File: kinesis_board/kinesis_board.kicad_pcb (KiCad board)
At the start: 2 copper layers, 106.7 x 144.8 mm, 40 parts, among them J1 RIGHT_13_TOP, J10 LEFT_13_DOWN, J2 RIGHT_13_DOWN, J3 THUMB_RIGHT_SPC_KB600, J4 THUMB_RIGHT_SPC, J5 THUMB_LEFT_BAK, J6 THUMB_LEFT_BAK_KB600, J7 LEFT_1x24, J8 RIGHT_1x24, J9 LEFT_13_TOP

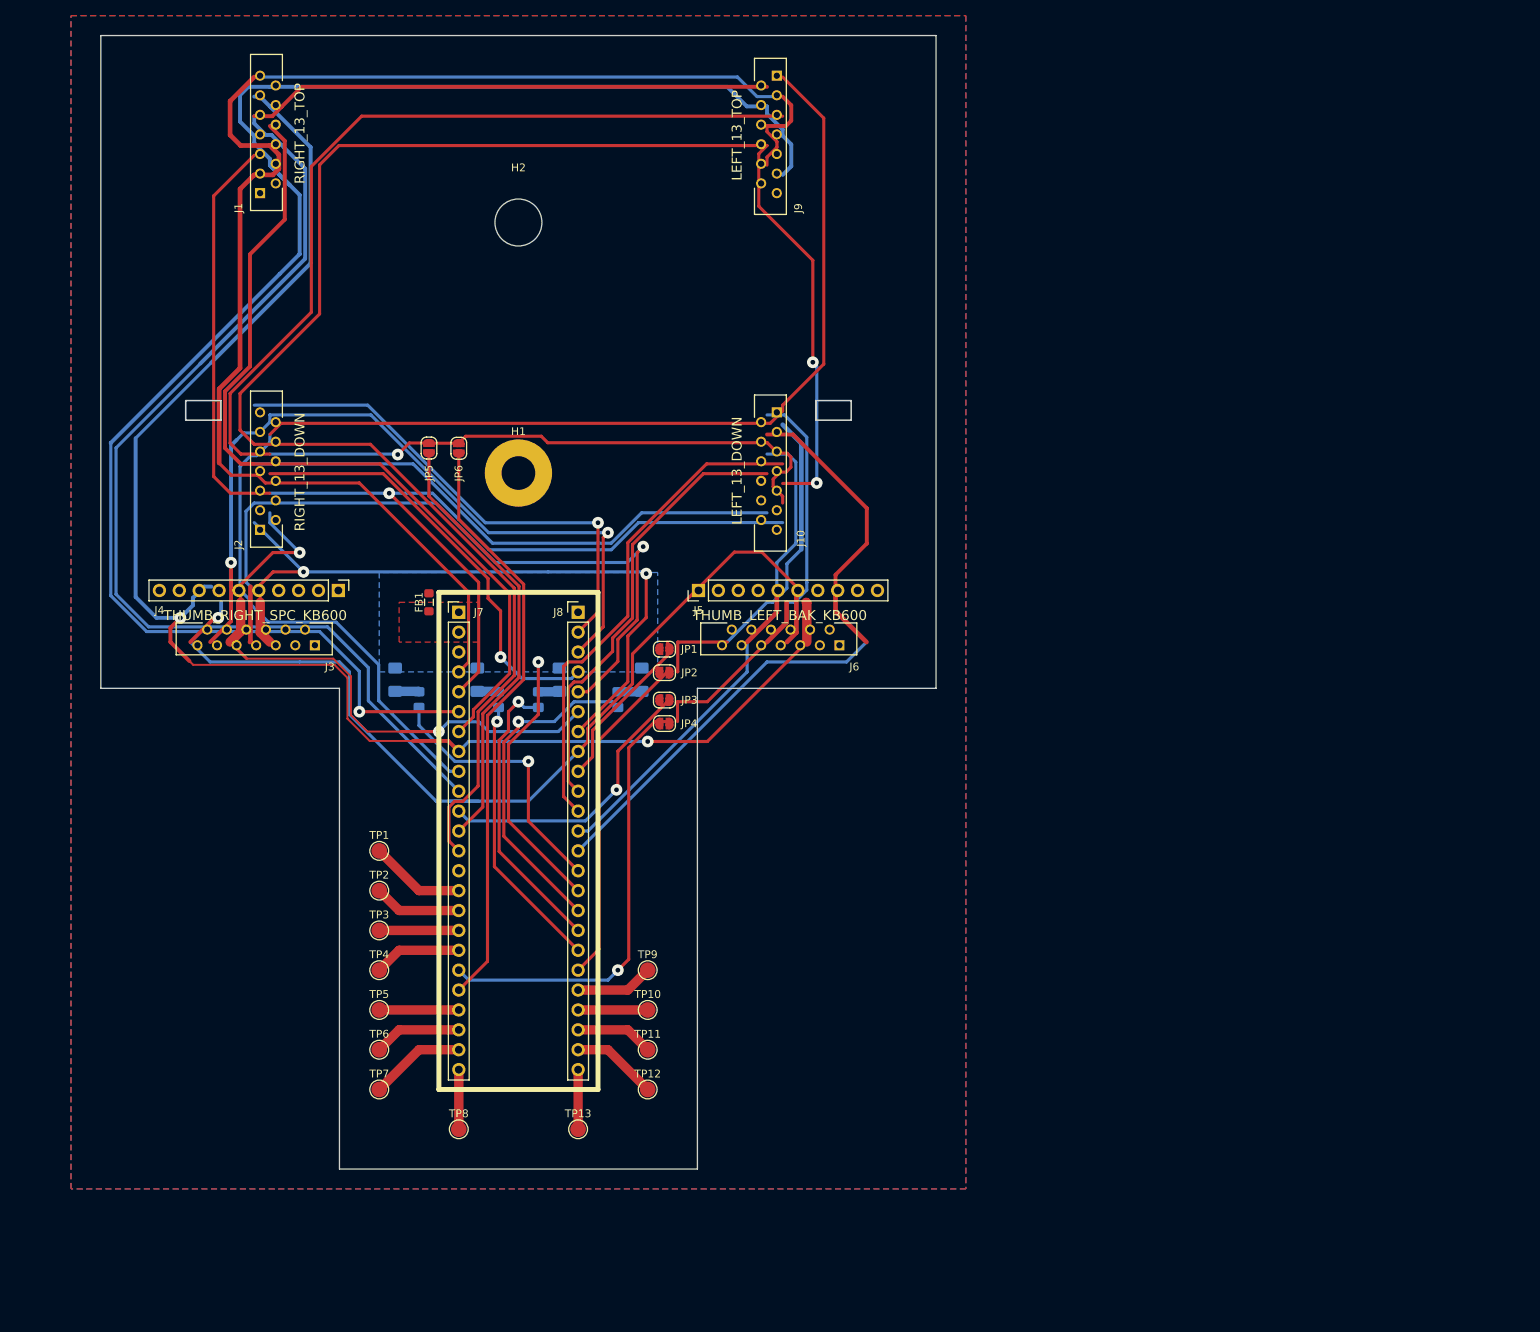
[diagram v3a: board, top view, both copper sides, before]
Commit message: finished routing of revision 2.0
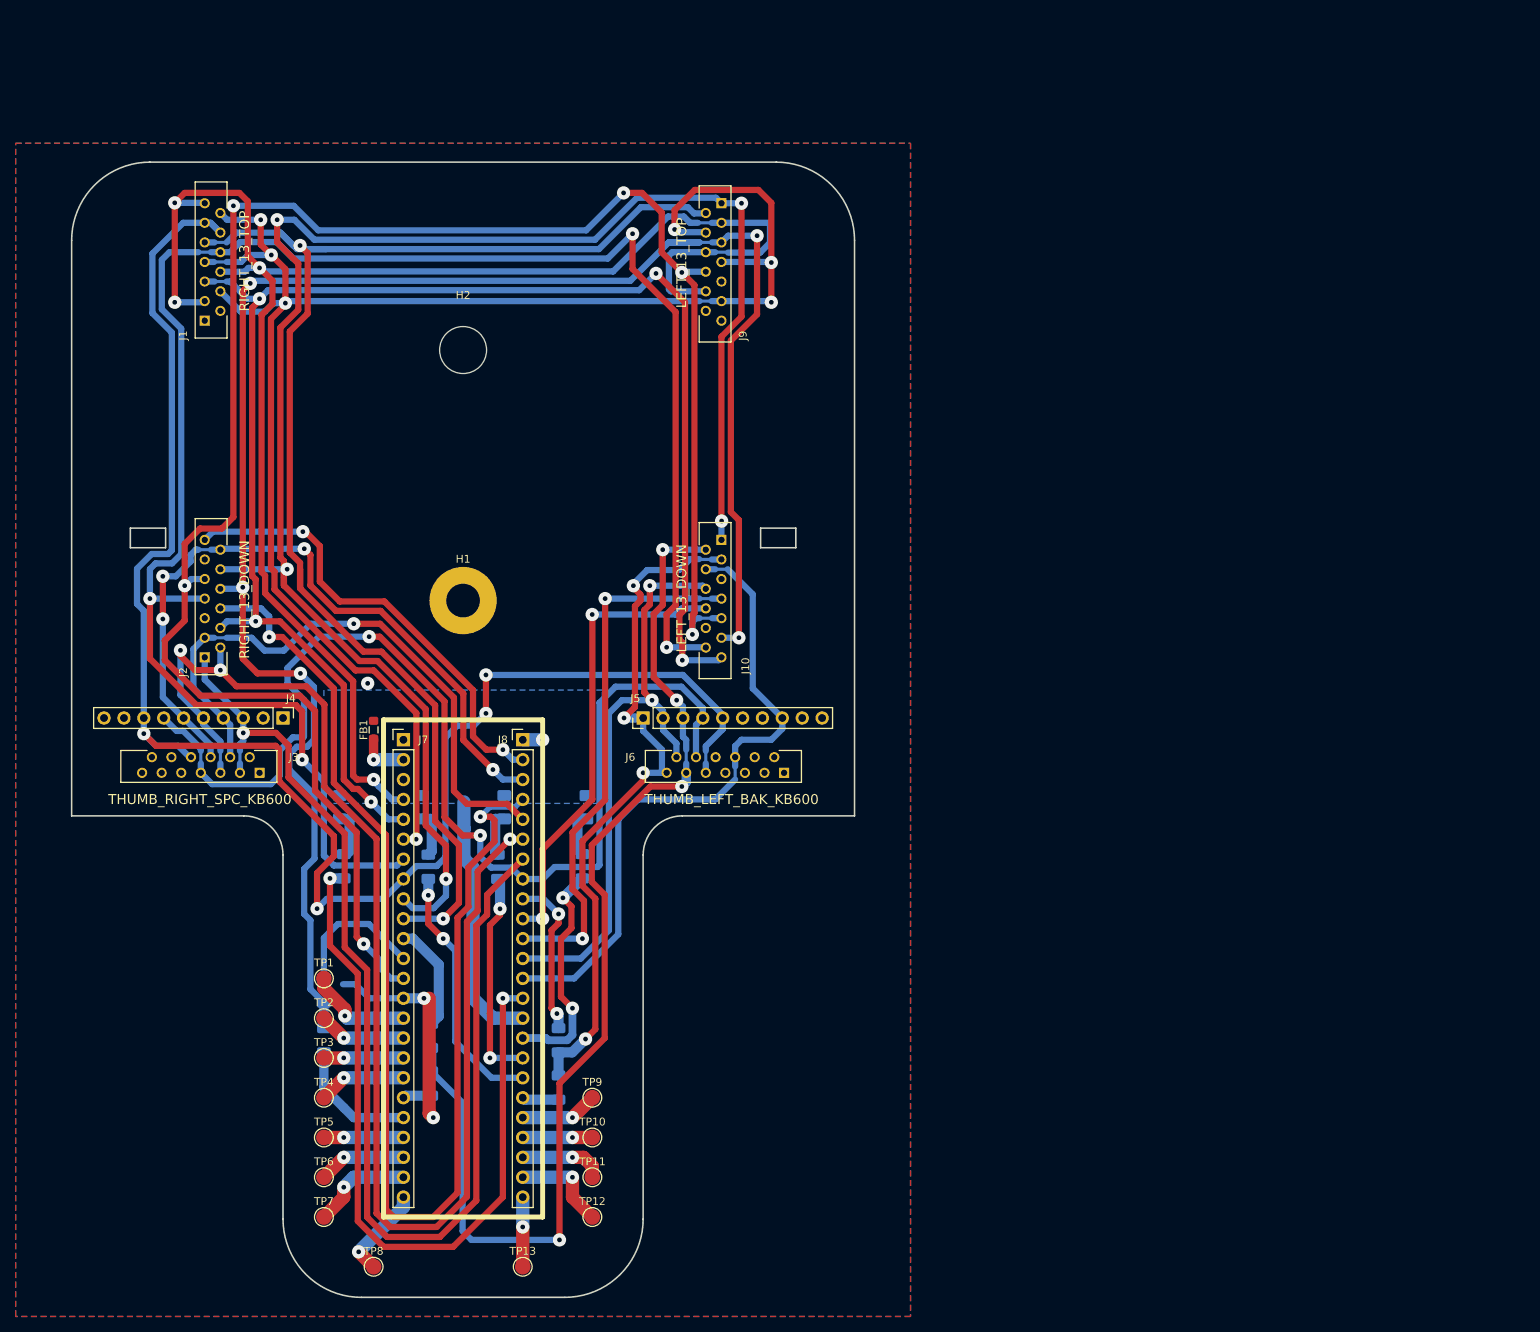
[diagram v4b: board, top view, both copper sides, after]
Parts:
- removed JP1, JP2, JP3, JP4, JP5, JP6: SolderJumper_2_Open, Jumper:SolderJumper-2_P1.3mm_Open_RoundedPad1.0x1.5mm
- added R10: 0R, Resistor_SMD:R_1206_3216Metric_Pad1.30x1.75mm_HandSolder, B.Cu at (74.2, 143.6)
- added R5: 0R, Resistor_SMD:R_1206_3216Metric_Pad1.30x1.75mm_HandSolder, B.Cu at (104.2, 156.0)
- added R6: 0R, Resistor_SMD:R_1206_3216Metric_Pad1.30x1.75mm_HandSolder, B.Cu at (104.2, 149.9)
- added R7: 0R, Resistor_SMD:R_1206_3216Metric_Pad1.30x1.75mm_HandSolder, B.Cu at (87.9, 155.5)
- added R8: 0R, Resistor_SMD:R_1206_3216Metric_Pad1.30x1.75mm_HandSolder, B.Cu at (87.9, 149.4)
- added R9: 0R, Resistor_SMD:R_1206_3216Metric_Pad1.30x1.75mm_HandSolder, B.Cu at (74.2, 149.9)
- R1, R2, R3, R4: footprint Resistor_SMD:R_0805_2012Metric_Pad1.20x1.40mm_HandSolder -> Resistor_SMD:R_1206_3216Metric_Pad1.30x1.75mm_HandSolder
- moved R4 23.4 mm to (76.8, 127.7)
- moved R3 23.2 mm to (87.5, 127.8)
- moved R2 22.0 mm to (96.4, 127.8)
- moved R1 21.8 mm to (107.2, 127.7)
- moved TP8 20.7 mm to (80.6, 178.8)
- moved TP13 18.9 mm to (99.6, 178.8)
- moved TP3 17.8 mm to (74.2, 152.2)
- moved H1 17.8 mm to (92.0, 93.8)
- moved J2 17.8 mm to (59.0, 101.0)
- moved J3 17.8 mm to (66.0, 115.8)
- moved J4 17.8 mm to (69.0, 108.8)
- moved J5 17.8 mm to (115.0, 108.8)
- moved J8 17.8 mm to (99.6, 111.5)
- moved TP1 17.8 mm to (74.2, 142.0)
- moved H2 17.8 mm to (92.0, 61.8)
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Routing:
- net /ROW_MIN: track 55.5 -> 158.2 mm, vias 1 -> 2
- net /ROW_8: track 78.0 -> 172.9 mm, vias 2 -> 3
- net /ROW_5: track 60.3 -> 144.2 mm, vias 0 -> 4
- net /LED_CAPS_LOCK: track 34.8 -> 97.5 mm, vias 1 -> 2
- net /ROW_6: track 90.6 -> 151.3 mm, vias 2 -> 1
- net /COL_2_JUMP1: track 75.4 -> 16.3 mm
- net /COL_3: track 180.8 -> 238.7 mm, vias 0 -> 4
- net /ROW_5_JUMP1: track 56.7 -> 3.66 mm, vias 1 -> 0
- net /COL_2: track 184.6 -> 236.7 mm, vias 1 -> 5
- net /COL_0: track 176.1 -> 223.5 mm, vias 0 -> 5
- net /COL_4: track 152.3 -> 199.5 mm, vias 1 -> 5
- net /ROW_4: track 43.2 -> 89.6 mm, vias 0 -> 4
- net /COL_2_JUMP0: track 56.2 -> 17.9 mm
- net /ROW_4_JUMP1: track 42.8 -> 4.68 mm
- net /ROW_2: track 42.5 -> 77.6 mm, vias 0 -> 2
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- removed copper zone on F.Cu, net GNDA
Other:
- board size 106.7 x 144.8 mm -> 100 x 145 mm

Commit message: adjusted size of the board
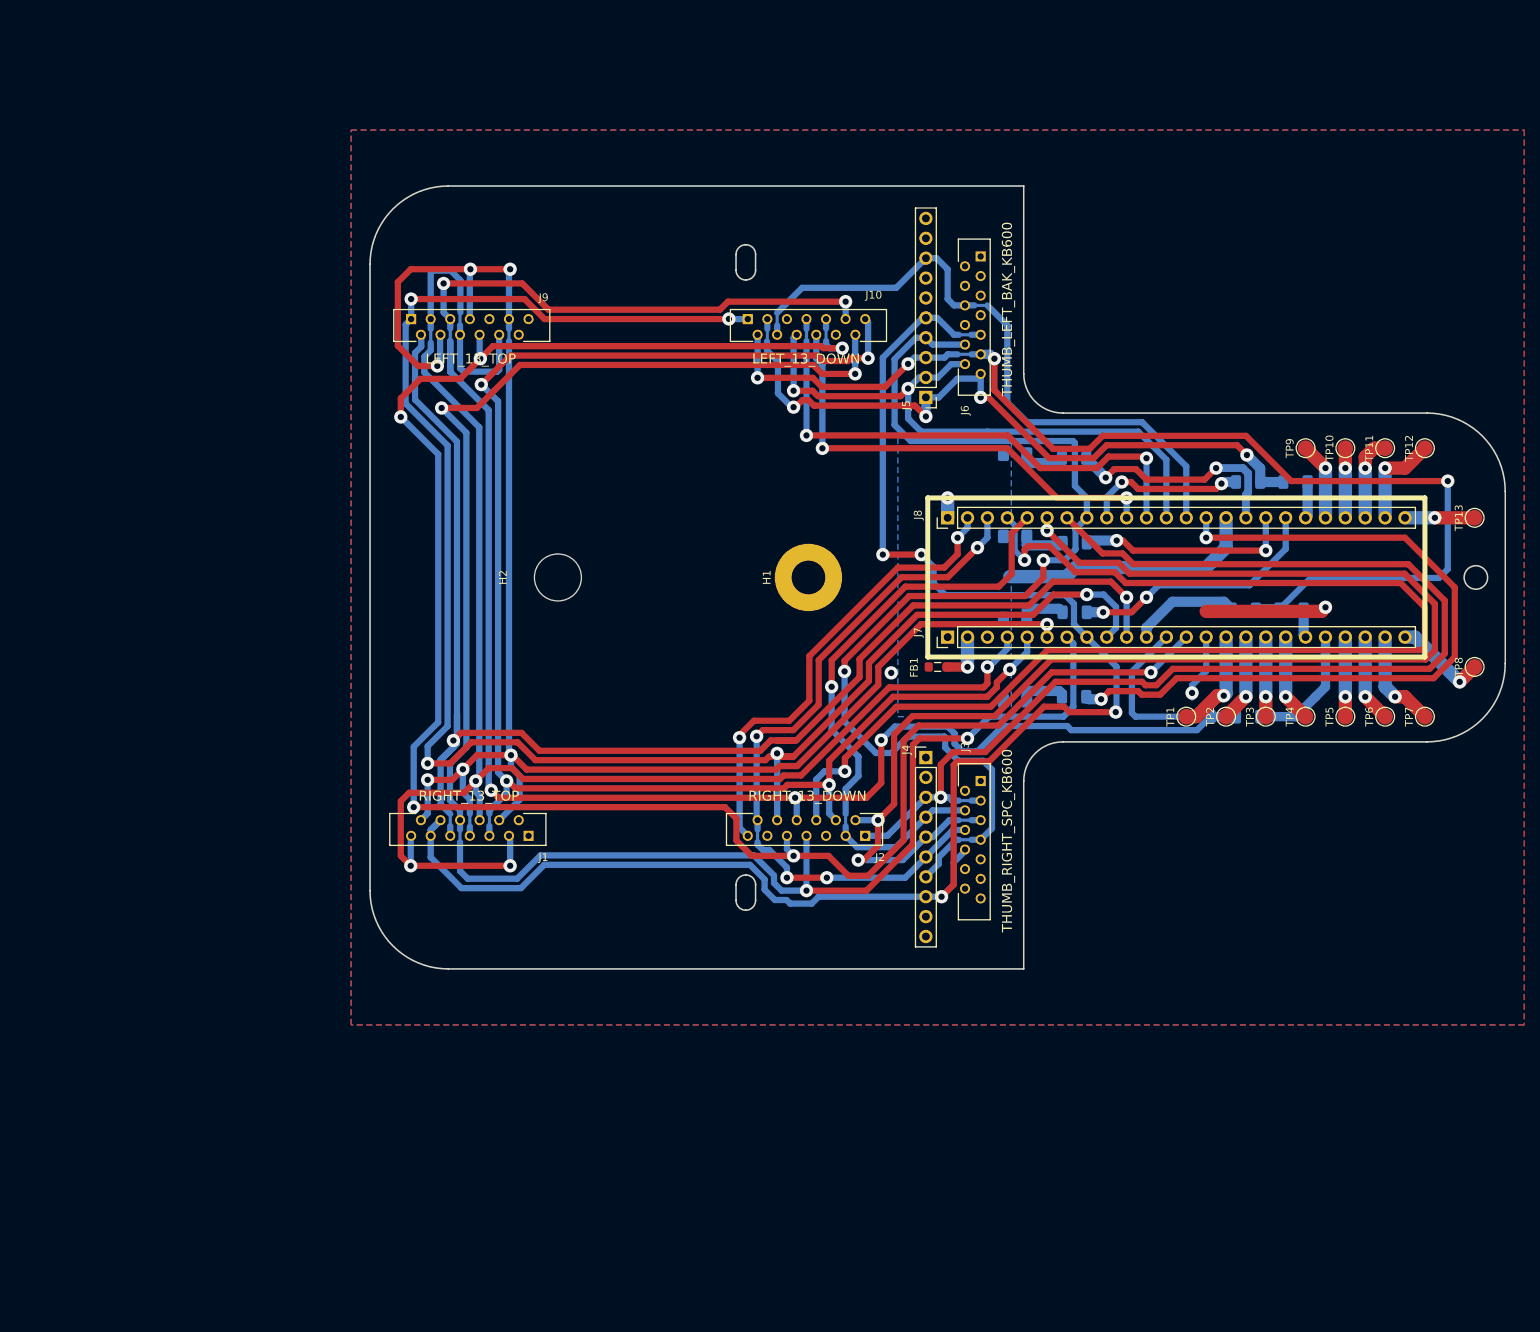
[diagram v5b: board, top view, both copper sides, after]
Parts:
- moved TP8 160.1 mm to (221.2, 102.2), turned to 90 degrees
- moved TP13 154.7 mm to (221.2, 83.2), turned to 90 degrees
- moved TP7 154.5 mm to (214.8, 108.6), turned to 90 degrees
- moved TP6 147.8 mm to (209.8, 108.6), turned to 90 degrees
- moved TP12 144.7 mm to (214.8, 74.3), turned to 90 degrees
- moved TP5 141.1 mm to (204.7, 108.6), turned to 90 degrees
- moved TP11 137.6 mm to (209.8, 74.3), turned to 90 degrees
- moved TP4 134.5 mm to (199.6, 108.6), turned to 90 degrees
- moved TP10 130.4 mm to (204.7, 74.3), turned to 90 degrees
- moved TP3 128.0 mm to (194.5, 108.6), turned to 90 degrees
- moved R7 125.5 mm to (197.8, 94.9), turned to 180 degrees
- moved R9 125.1 mm to (192.3, 108.6), turned to 180 degrees
- moved TP9 123.2 mm to (199.6, 74.3), turned to 90 degrees
- moved R5 121.8 mm to (198.3, 78.6), turned to 180 degrees
- moved TP2 121.5 mm to (189.4, 108.6), turned to 90 degrees
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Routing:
- net GND: track 29.1 -> 26.5 mm
- net /COL_5: track 213.8 -> 211.6 mm
- net /LED_CAPS_LOCK: track 97.5 -> 95.6 mm
- net /COL_1: track 251.2 -> 250.3 mm
- net /COL_2_JUMP0: track 17.9 -> 18.7 mm
- net /COL_2: track 236.7 -> 236.1 mm
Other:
- board size 100 x 145 mm -> 145 x 100 mm
